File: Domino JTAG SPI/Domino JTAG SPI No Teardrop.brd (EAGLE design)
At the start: 25.4 x 33 mm, 34 parts, among them J1 MH8-1, J2 MH10-1, J3 MH10-1, J4 MH2-1, J5 MH8-1, J6 MHRA7-2-0.1, SW1 IT-1124SMD, U1 SPI_FLASH

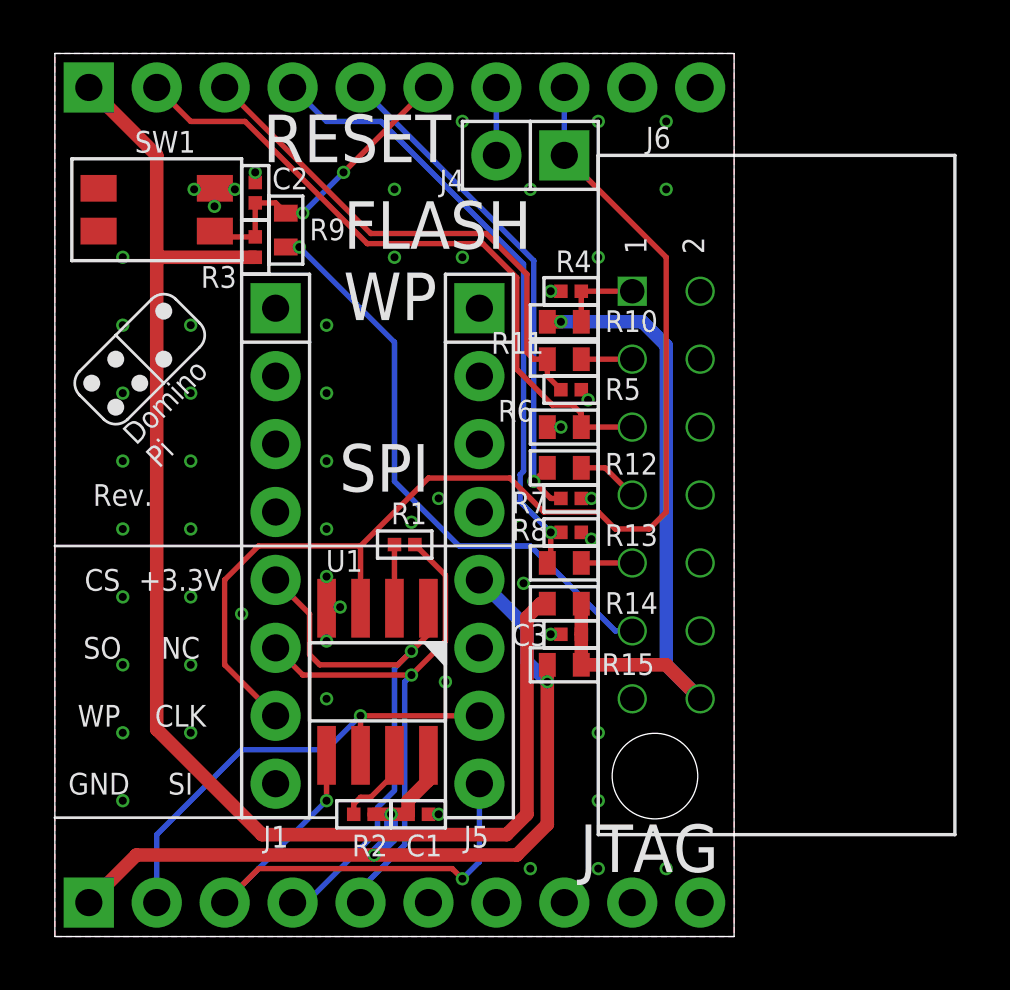
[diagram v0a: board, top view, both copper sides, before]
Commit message: Changed Domino JTAG SPI to Rev. C
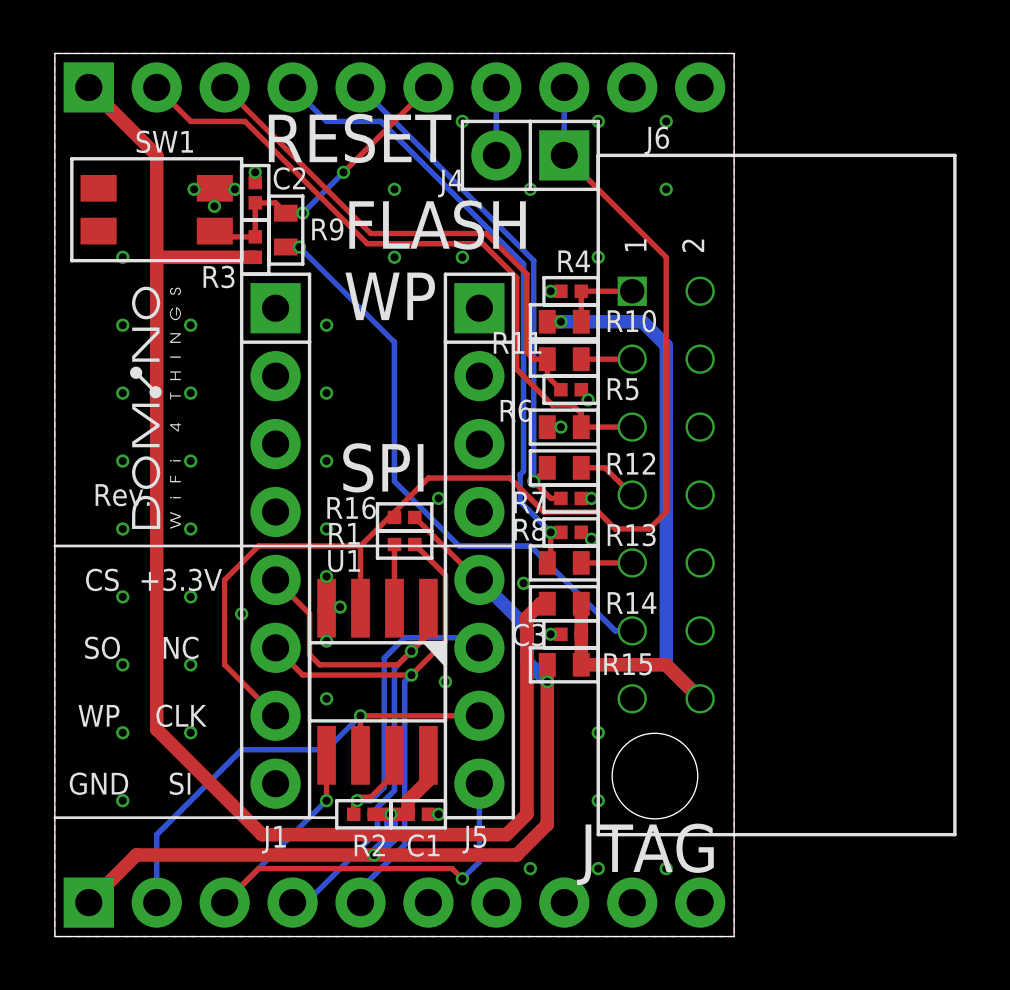
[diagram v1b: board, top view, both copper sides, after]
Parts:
- removed U$17: (no value), Domino:DOMINO_LOGO_SMALL
- added R16: 10k, Domino:R0402
- added U$11: (no value), Domino:DOMINO_LOGO
- added U$2: DOMINO_LOGO_SMALL, Domino:DOMINO_LOGO_SMALL
- R1: value 1k -> 0R
- moved U$10 9.09 mm to (14.9, 18.7)
- moved U$4 2.01 mm to (12.8, 26.2)
- moved U$8 1.27 mm to (6.73, 18.5)
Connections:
- removed net N$4: R2.2, U1.7
- new net !SPI_HOLD: J5.6, R2.2, U1.7
- net +3V3: now also R16.1
- net FLASH_WP: now also R16.2
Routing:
- net !SPI_HOLD: track 0.00 -> 13.1 mm, vias 0 -> 1
- net +3V3: track 34.8 -> 38.1 mm
- net N$4: track 3.06 -> 0.00 mm
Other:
- board text removed: "Domino Core"
- board text removed: "Domino Pi"
- board text removed: "Domino Qi"

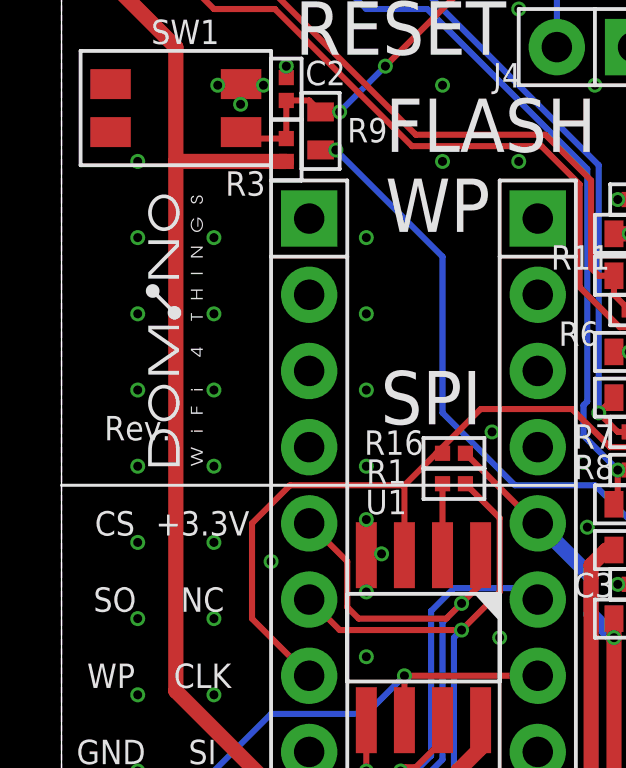
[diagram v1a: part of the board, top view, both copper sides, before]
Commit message: Domino JTAG SPI Rev. C: changed Logos
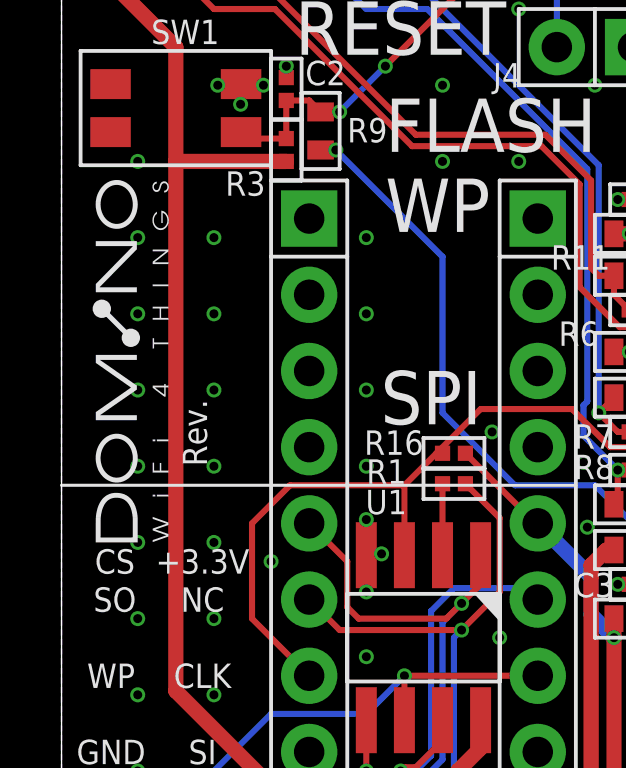
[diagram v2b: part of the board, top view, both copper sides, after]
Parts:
- removed U$4: (no value), Domino:DOMINO_LOGO_SMALL
- added U$12: (no value), Domino:DOMINO_LOGO_SMALL
- U$11: device Domino:DOMINO_LOGO -> Domino:DOMINO_LOGO_SMALL
- U$2: value DOMINO_LOGO_SMALL -> DOMINO_LOGO; device Domino:DOMINO_LOGO_SMALL -> Domino:DOMINO_LOGO
- moved U$2 79.8 mm to (-44.5, -48.3), turned to 0 degrees
- moved U$11 68.5 mm to (2.54, 12.7), turned to 90 degrees
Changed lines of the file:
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@@
 <layer number="54" name="bGND_GNDA" color="1" fill="9" visible="no" active="no"/>
 <layer number="56" name="wert" color="7" fill="1" visible="no" active="no"/>
+<layer number="90" name="Modules" color="5" fill="1" visible="no" active="yes"/>
 <layer number="91" name="Nets" color="2" fill="1" visible="no" active="no"/>
 <layer number="92" name="Busses" color="1" fill="1" visible="no" active="no"/>
@@
 <layer number="143" name="mvRestrict" color="7" fill="1" visible="no" active="no"/>
 <layer number="144" name="DrillLegend" color="7" fill="1" visible="yes" active="yes"/>
-<layer number="145" name="DrillLegend_01-16" color="2" fill="9" visible="yes" active="yes"/>
-<layer number="146" name="DrillLegend_01-20" color="3" fill="9" visible="yes" active="yes"/>
+<layer number="145" name="DrillLegend_01-16" color="2" fill="9" visible="no" active="yes"/>
+<layer number="146" name="DrillLegend_01-20" color="3" fill="9" visible="no" active="yes"/>
 <layer number="147" name="mMeasures" color="7" fill="1" visible="no" active="no"/>
 <layer number="148" name="mDocument" color="7" fill="1" visible="no" active="no"/>
@@
 <dimension x1="25.4" y1="33.02" x2="0" y2="33.02" x3="12.7" y3="35.56" textsize="1.778" layer="47" dtype="horizontal"/>
 <text x="3.81" y="29.21" size="0.8128" layer="22" rot="MR90" align="center">TDO</text>
-<text x="1.27" y="27.686" size="0.8128" layer="22" rot="MR90" align="center">+2V5</text>
-<text x="1.27" y="13.843" size="0.8128" layer="26" rot="MR270" align="center">&gt;DATE</text>
-<text x="1.27" y="7.62" size="0.8128" layer="26" rot="MR90" align="center">Rev.</text>
+<text x="1.27" y="28.956" size="0.8128" layer="22" rot="MR90" align="center">+2V5</text>
+<text x="5.588" y="8.89" size="0.8128" layer="26" rot="MR0" align="center-left">&gt;DATE</text>
+<text x="5.715" y="10.16" size="0.8128" layer="26" rot="MR0" align="center-left">Rev.</text>
 <text x="1.27" y="34.29" size="1.27" layer="150" rot="R90" align="center-left">+2V5</text>
 <text x="3.81" y="34.29" size="1.27" layer="150" rot="R90" align="center-left">JTAG_TDO</text>
@@
 <text x="12.319" y="17.526" size="1.778" layer="21" align="center">SPI</text>
 <text x="22.225" y="3.302" size="1.778" layer="21" rot="R180" align="center">JTAG</text>
-<text x="1.27" y="9.525" size="0.8128" layer="26" rot="MR90" align="center">&gt;REV</text>
+<text x="3.175" y="10.16" size="0.8128" layer="26" rot="MR0" align="center-left">&gt;REV</text>
 <text x="24.13" y="3.81" size="0.8128" layer="22" rot="MR90" align="center">GND</text>
 <text x="13.97" y="4.445" size="0.8128" layer="22" rot="MR90" align="center">GND</text>
@@
 <text x="6.35" y="3.175" size="0.8128" layer="22" rot="MR0" align="center">MOSI</text>
 <text x="3.81" y="4.445" size="0.8128" layer="22" rot="MR270" align="center">CLK</text>
-<text x="3.683" y="15.24" size="0.8128" layer="25" rot="R180" align="center">&gt;DATE</text>
-<text x="4.445" y="16.51" size="0.8128" layer="25" align="center">&gt;REV</text>
-<text x="2.54" y="16.51" size="0.8128" layer="25" align="center">Rev.</text>
+<text x="5.715" y="15.367" size="0.8128" layer="25" rot="R90" align="center-left">&gt;DATE</text>
+<text x="4.445" y="17.78" size="0.8128" layer="25" rot="R90" align="center-left">&gt;REV</text>
+<text x="4.445" y="15.24" size="0.8128" layer="25" rot="R90" align="center-left">Rev.</text>
 <text x="10.795" y="25.273" size="1.778" layer="21" align="center-left">FLASH
 WP</text>
@@
 <text x="1.778" y="10.795" size="0.8128" layer="21" rot="R180" align="center">SO</text>
 <text x="4.699" y="8.255" size="0.8128" layer="21" align="center">CLK</text>
-<text x="1.778" y="13.335" size="0.8128" layer="21" rot="R180" align="center">CS</text>
-<text x="4.699" y="13.335" size="0.8128" layer="21" align="center">+3.3V</text>
+<text x="1.778" y="12.065" size="0.8128" layer="21" rot="R180" align="center">CS</text>
+<text x="4.699" y="12.065" size="0.8128" layer="21" align="center">+3.3V</text>
 <text x="4.699" y="5.715" size="0.8128" layer="21" align="center">SI</text>
 <text x="1.651" y="5.715" size="0.8128" layer="21" rot="R180" align="center">GND</text>
@@
 </plain>
 <attributes>
-<attribute name="DATE" value="20140827"/>
+<attribute name="DATE" value="20141230"/>
 <attribute name="DRAWN" value="M.STEMPIN"/>
-<attribute name="REV" value="B"/>
+<attribute name="REV" value="C"/>
 </attributes>
 <variantdefs>
@@
 <attribute name="PARTNO" value="IT-1124SMD" x="3.81" y="27.178" size="1.778" layer="27" rot="R180" display="off"/>
 </element>
-<element name="U$4" library="Domino" package="DOMINO_LOGO_SMALL" value="" x="12.827" y="26.162" rot="MR0"/>
 <element name="J2" library="Domino" package="MH10-1-0.1" value="MH10-1" x="1.27" y="31.75" smashed="yes" rot="MR180">
 <attribute name="PARTNO" value="MH10-1-0.1" x="1.27" y="31.75" size="1.778" layer="28" rot="MR180" display="off"/>
@@
 <attribute name="VALUE" x="14.351" y="17.5768" size="0.8128" layer="27" rot="R180"/>
 </element>
-<element name="U$2" library="Domino" package="DOMINO_LOGO_SMALL" value="DOMINO_LOGO_SMALL" x="3.937" y="15.24" rot="R90">
-<attribute name="BOM" value="EXCLUDE" x="3.937" y="15.24" size="1.778" layer="27" rot="R90" display="off"/>
-</element>
-<element name="U$11" library="Domino" package="DOMINO_LOGO" value="" x="-29.845" y="-47.625"/>
 <element name="DRILEGEND" library="drilegend" package="DRILEGEND" value="" x="81.534" y="59.944"/>
+<element name="U$2" library="Domino" package="DOMINO_LOGO" value="DOMINO_LOGO" x="-44.45" y="-48.26">
+<attribute name="BOM" value="EXCLUDE" x="-44.45" y="-48.26" size="1.778" layer="27" display="off"/>
+</element>
+<element name="U$11" library="Domino" package="DOMINO_LOGO_SMALL" value="" x="2.54" y="12.7" rot="R90"/>
+<element name="U$12" library="Domino" package="DOMINO_LOGO_SMALL" value="" x="12.7" y="25.4" rot="MR0"/>
 </elements>
 <signals>

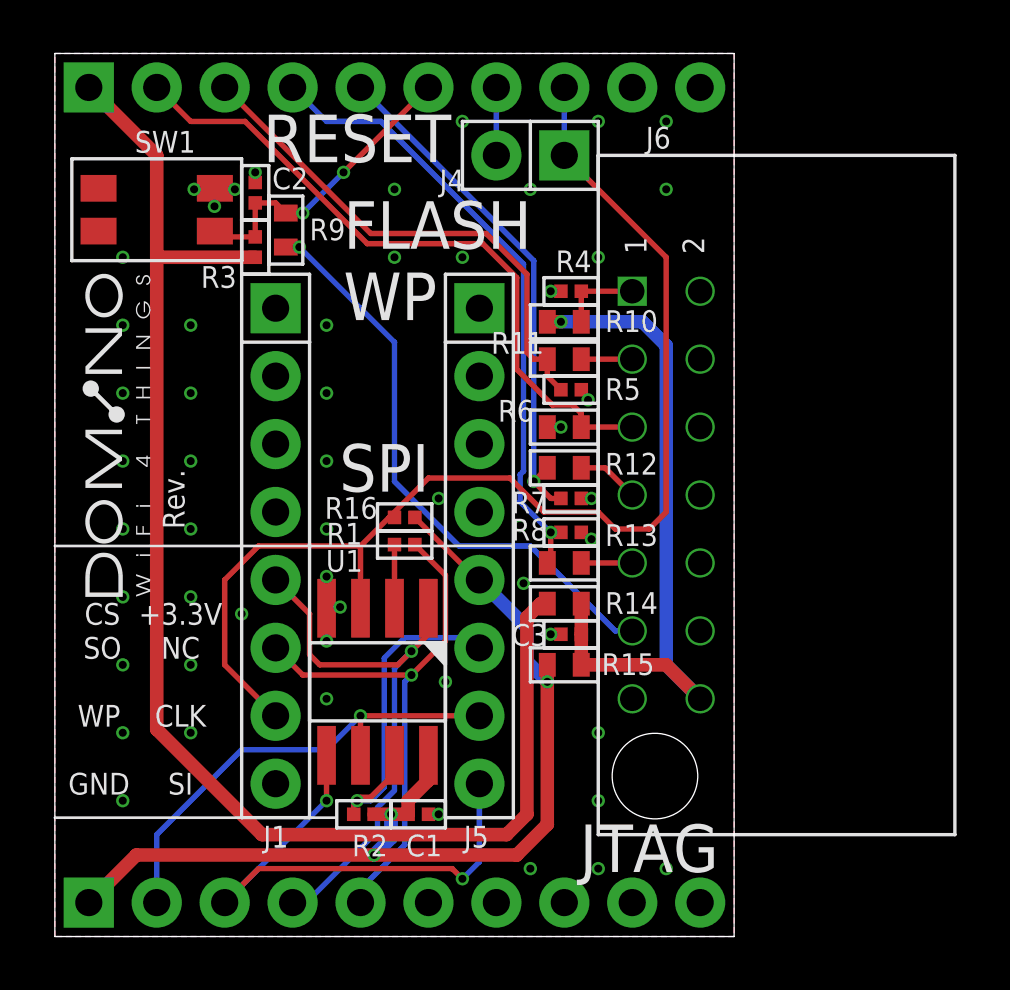
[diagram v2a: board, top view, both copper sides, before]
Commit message: Domino JTAG SPI Rev. D: changed silkscreen font ratio to 20%
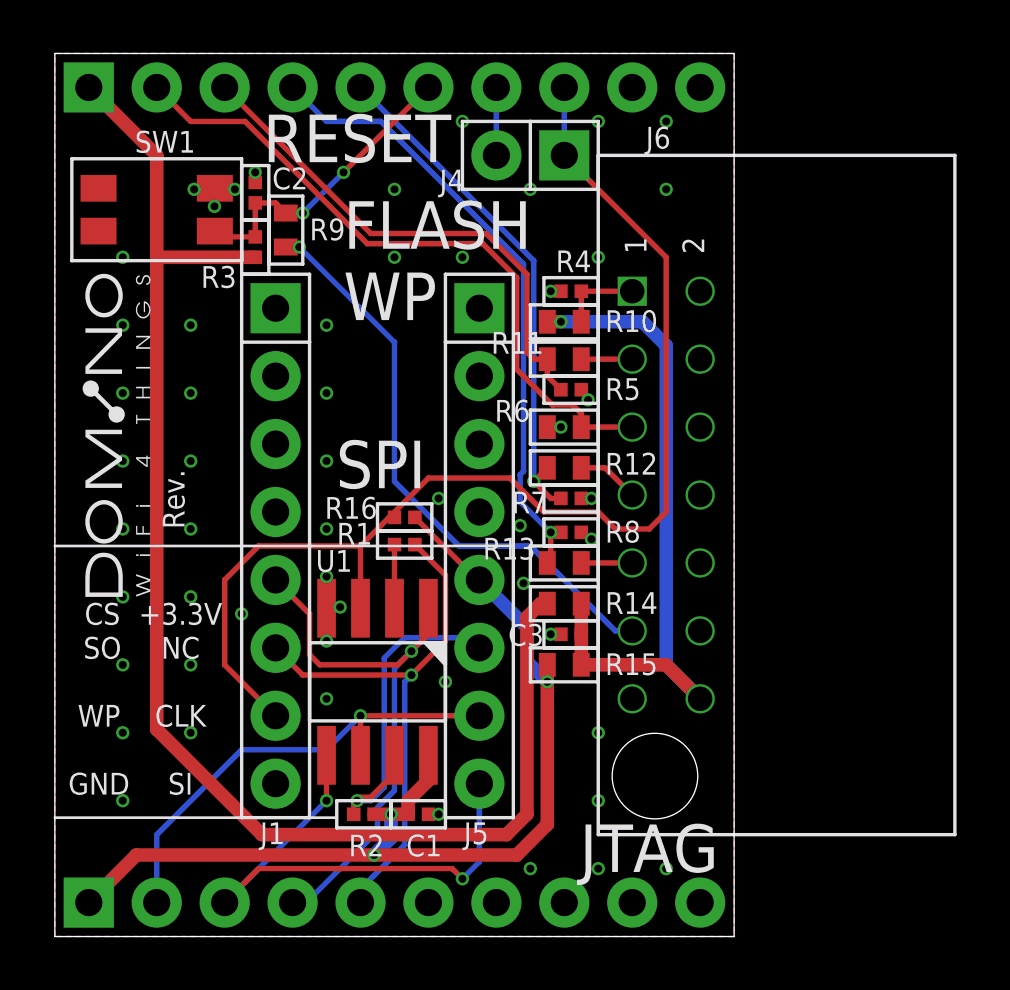
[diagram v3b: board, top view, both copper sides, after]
